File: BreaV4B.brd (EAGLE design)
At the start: 30.8 x 19 mm, 32 parts, among them J1 XF2L-0535-1, J2 XF2L-0535-1, Q3 ABM-16MHZ, SW1 ESE31L11T, SW2 EVQ11U09K, SW3 LS12T2-T, U1 TPS62200, X1 22-23-2021

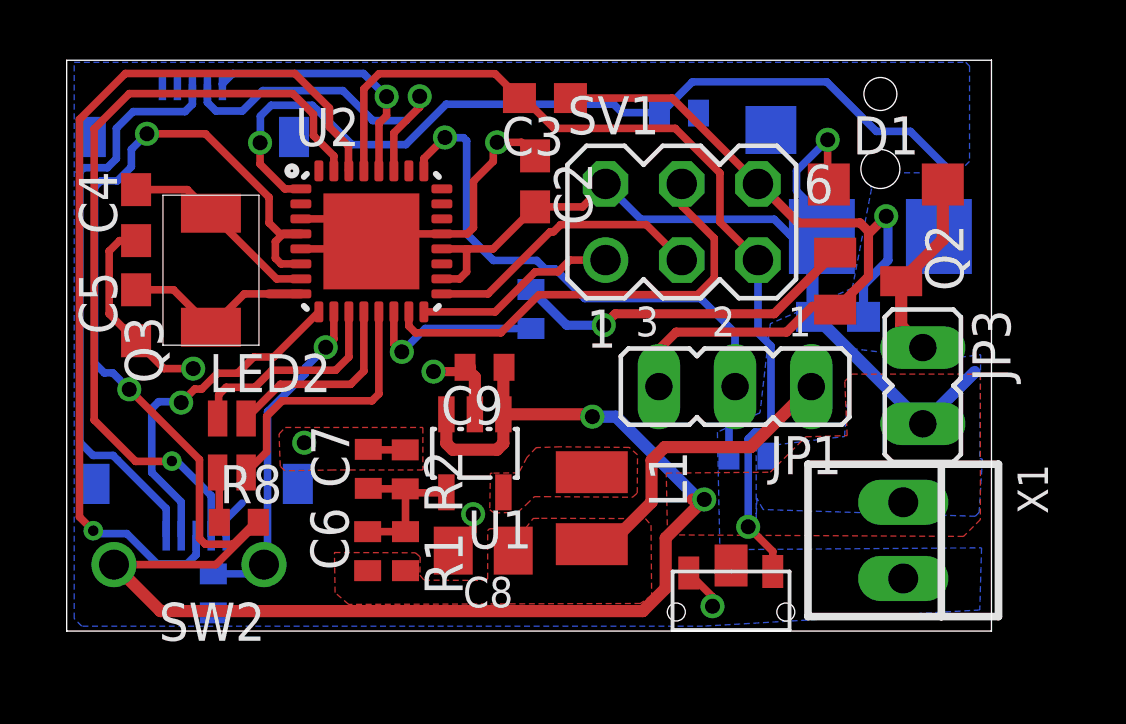
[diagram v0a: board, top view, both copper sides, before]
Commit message: Changes direction of GSM FPC. Lowered position of MQ303
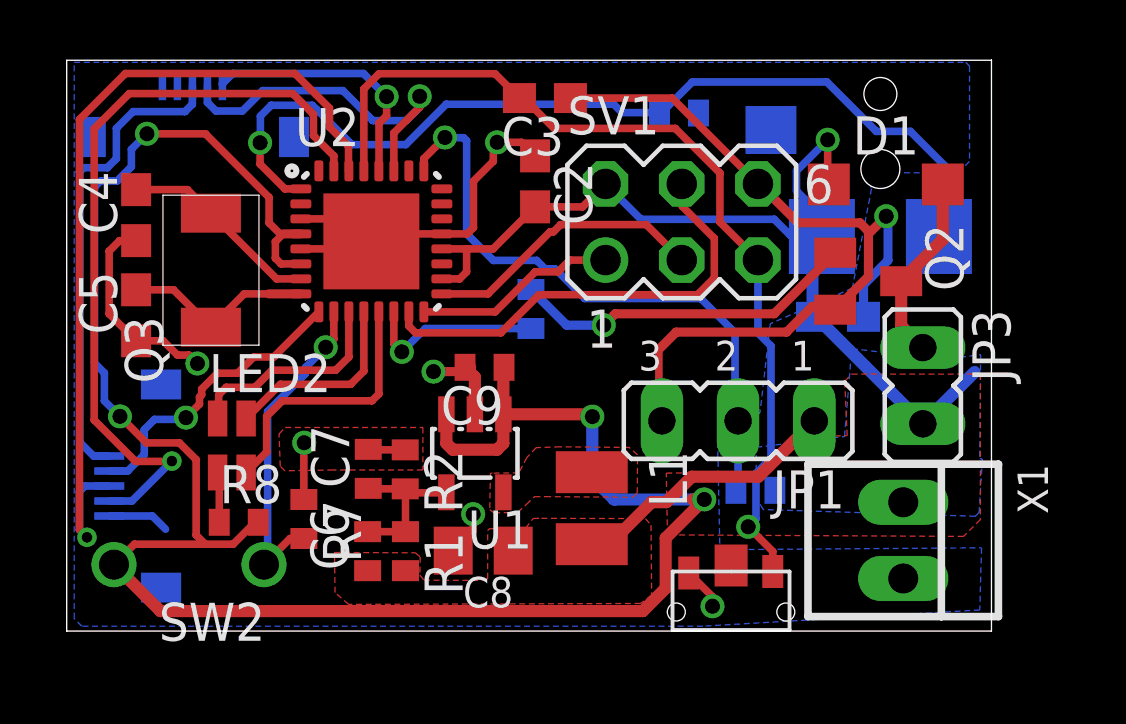
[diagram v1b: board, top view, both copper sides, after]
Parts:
- moved R7 3.91 mm to (7.91, 3.70), flipped to the top, turned to 270 degrees
- moved R3 1.16 mm to (23.0, 4.66)
- moved JP1 1.14 mm to (22.4, 6.97)
- moved J1 1.02 mm to (3.33, 4.80), turned to 0 degrees
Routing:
- net GND: track 56.5 -> 60.4 mm
- net VBATSIM: track 19.6 -> 16.1 mm
- net RX: track 30.4 -> 28.5 mm
- net REST: track 11.6 -> 9.92 mm
- net VOUT: track 10.6 -> 9.38 mm
- net N$3: track 19.8 -> 20.9 mm

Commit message: TrussKey Schematics
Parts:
- R8: value 10K -> 1K
- moved SW2 1.04 mm to (5.07, 2.50)
- moved J1 0.93 mm to (4.26, 4.87)
- moved R7 0.61 mm to (8.14, 4.26), turned to 180 degrees
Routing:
- net VCC: track 101.8 -> 100.4 mm
- net GND: track 60.4 -> 61.7 mm
- net REST: track 9.92 -> 8.90 mm
- net RX: track 28.5 -> 29.5 mm
- net VBATSIM: track 16.1 -> 17.0 mm
- net TX: track 25.9 -> 25.1 mm

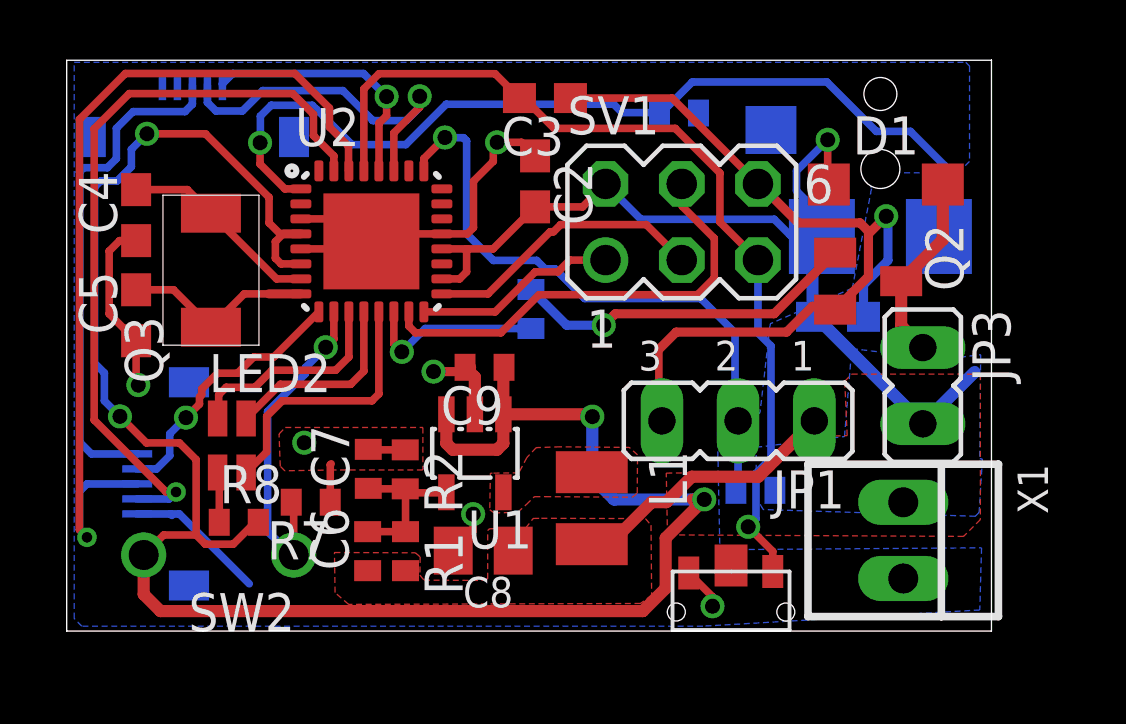
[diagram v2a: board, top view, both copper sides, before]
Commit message: Power Switch to int0
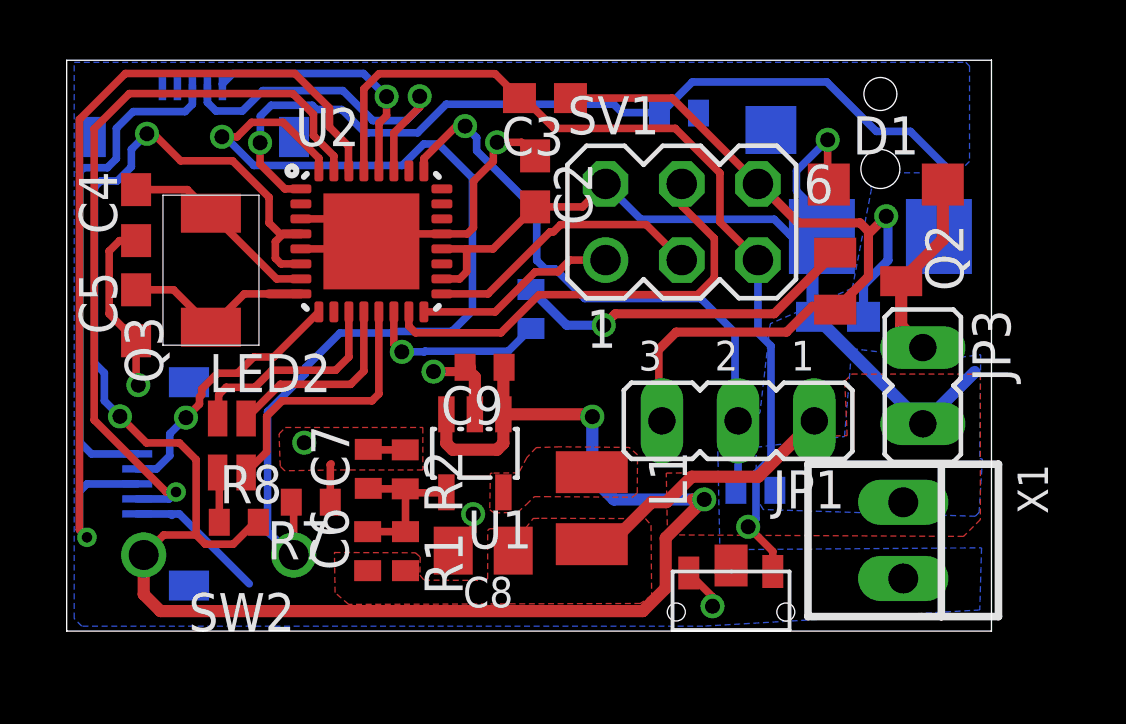
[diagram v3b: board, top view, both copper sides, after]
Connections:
- net PWRSW: now also U2.32; no longer U2.10
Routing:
- net PWRSW: track 11.2 -> 33.6 mm
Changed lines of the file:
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@@
 <wire x1="7.81" y1="13.204" x2="7.116" y2="13.204" width="0.254" layer="1"/>
 <wire x1="7.116" y1="13.204" x2="6.75" y2="13.57" width="0.254" layer="1"/>
-<wire x1="6.75" y1="13.57" x2="6.75" y2="14.42" width="0.254" layer="1"/>
-<wire x1="4.63" y1="16.54" x2="2.68" y2="16.54" width="0.254" layer="1"/>
+<wire x1="6.75" y1="14.42" x2="6.75" y2="13.57" width="0.254" layer="1"/>
 <via x="2.68" y="16.54" extent="1-16" drill="0.5"/>
 <wire x1="2.68" y1="16.54" x2="2.16" y2="16.02" width="0.254" layer="16"/>
@@
 <wire x1="0.93" y1="14.76" x2="0.93" y2="8.9" width="0.254" layer="16"/>
 <via x="1.78" y="7.12" extent="1-16" drill="0.5"/>
-<wire x1="4.63" y1="16.54" x2="6.75" y2="14.42" width="0.254" layer="1"/>
 <wire x1="21.256" y1="4.352" x2="21.0734" y2="4.352" width="0.4064" layer="16"/>
 <wire x1="20.872" y1="4.352" x2="21.256" y2="4.352" width="0.4064" layer="1"/>
@@
 <wire x1="2.57" y1="2.5" x2="3.23611875" y2="3.16611875" width="0.254" layer="1"/>
 <wire x1="3.23611875" y1="3.16611875" x2="4.31875" y2="3.16611875" width="0.254" layer="1"/>
+<wire x1="2.68" y1="16.54" x2="2.9" y2="16.54" width="0.254" layer="1"/>
+<wire x1="3.8" y1="15.64" x2="5.53" y2="15.64" width="0.254" layer="1"/>
+<wire x1="5.53" y1="15.64" x2="6.75" y2="14.42" width="0.254" layer="1"/>
+<wire x1="2.9" y1="16.54" x2="3.8" y2="15.64" width="0.254" layer="1"/>
 </signal>
 <signal name="N$1">
@@
 <contactref element="R3" pad="1"/>
 <contactref element="U2" pad="25"/>
-<via x="12.613" y="16.417" extent="1-16" drill="0.5"/>
+<via x="13.283" y="16.797" extent="1-16" drill="0.5"/>
 <wire x1="17.272" y1="11.049" x2="21.141" y2="11.049" width="0.254" layer="16"/>
-<wire x1="14.224" y1="12.319" x2="13.335" y2="13.208" width="0.254" layer="16"/>
-<wire x1="14.224" y1="12.319" x2="15.6718" y2="12.319" width="0.254" layer="16"/>
 <wire x1="15.6718" y1="12.319" x2="15.9512" y2="12.0396" width="0.254" layer="16"/>
 <wire x1="15.9512" y1="12.0396" x2="16.2814" y2="12.0396" width="0.254" layer="16"/>
@@
 <wire x1="21.141" y1="11.049" x2="22.284" y2="9.906" width="0.254" layer="16"/>
 <wire x1="11.91" y1="15.304" x2="11.91" y2="15.714" width="0.254" layer="1"/>
-<wire x1="11.91" y1="15.714" x2="12.613" y2="16.417" width="0.254" layer="1"/>
-<wire x1="13.335" y1="13.208" x2="13.335" y2="16.305" width="0.254" layer="16"/>
-<wire x1="13.335" y1="16.305" x2="13.23" y2="16.41" width="0.254" layer="16"/>
-<wire x1="13.23" y1="16.41" x2="12.62" y2="16.41" width="0.254" layer="16"/>
-<wire x1="12.62" y1="16.41" x2="12.613" y2="16.417" width="0.254" layer="16"/>
 <wire x1="22.284" y1="9.906" x2="22.284" y2="7.072" width="0.254" layer="16"/>
 <wire x1="22.284" y1="7.072" x2="22.384" y2="6.972" width="0.254" layer="16"/>
 <wire x1="22.384" y1="6.972" x2="22.384" y2="4.73" width="0.254" layer="16"/>
 <wire x1="22.384" y1="4.73" x2="22.309" y2="4.655" width="0.254" layer="16"/>
+<wire x1="11.91" y1="15.714" x2="12.993" y2="16.797" width="0.254" layer="1"/>
+<wire x1="12.993" y1="16.797" x2="13.283" y2="16.797" width="0.254" layer="1"/>
+<wire x1="13.283" y1="16.797" x2="13.6692" y2="16.4108" width="0.254" layer="16"/>
+<wire x1="13.6692" y1="16.4108" x2="13.6692" y2="15.9735875" width="0.254" layer="16"/>
+<wire x1="15.6718" y1="13.9709875" x2="15.6718" y2="12.319" width="0.254" layer="16"/>
+<wire x1="13.6692" y1="15.9735875" x2="15.6718" y2="13.9709875" width="0.254" layer="16"/>
 </signal>
 <signal name="SW">
@@
 <signal name="SOL">
 <contactref element="R5" pad="2"/>
-<wire x1="15.479" y1="10.05" x2="11.955" y2="10.05" width="0.254" layer="16"/>
-<wire x1="11.955" y1="10.05" x2="11.176" y2="9.271" width="0.254" layer="16"/>
 <via x="11.176" y="9.271" extent="1-16" drill="0.5"/>
 <contactref element="U2" pad="14"/>
 <wire x1="10.91" y1="10.604" x2="10.91" y2="9.537" width="0.254" layer="1"/>
 <wire x1="10.91" y1="9.537" x2="11.176" y2="9.271" width="0.254" layer="1"/>
+<wire x1="11.176" y1="9.271" x2="11.9247875" y2="9.271" width="0.254" layer="16"/>
+<wire x1="11.9247875" y1="9.271" x2="11.9485875" y2="9.2948" width="0.254" layer="16"/>
+<wire x1="14.7238" y1="9.2948" x2="15.479" y2="10.05" width="0.254" layer="16"/>
+<wire x1="11.9485875" y1="9.2948" x2="14.7238" y2="9.2948" width="0.254" layer="16"/>
 </signal>
 <signal name="N$9">
@@
 <wire x1="28.13" y1="16.62" x2="29.28" y2="15.47" width="0.254" layer="16"/>
 <contactref element="U2" pad="1"/>
-<wire x1="18.2372" y1="17.526" x2="12.656" y2="17.526" width="0.254" layer="16"/>
-<wire x1="12.656" y1="17.526" x2="11.31" y2="16.18" width="0.254" layer="16"/>
-<wire x1="11.31" y1="16.18" x2="9.51" y2="16.18" width="0.254" layer="16"/>
-<wire x1="9.51" y1="16.18" x2="8.34" y2="17.35" width="0.254" layer="16"/>
-<wire x1="8.34" y1="17.35" x2="8.33" y2="17.35" width="0.254" layer="16"/>
-<wire x1="8.33" y1="17.35" x2="8.19" y2="17.49" width="0.254" layer="16"/>
+<wire x1="12.656" y1="17.526" x2="18.2372" y2="17.526" width="0.254" layer="16"/>
+<wire x1="8.19" y1="17.49" x2="8.33" y2="17.35" width="0.254" layer="16"/>
 <wire x1="8.19" y1="17.49" x2="6.82" y2="17.49" width="0.254" layer="16"/>
 <wire x1="7.81" y1="14.704" x2="7.276" y2="14.704" width="0.254" layer="1"/>
@@
 <wire x1="6.45" y1="16.24" x2="6.45" y2="15.53" width="0.254" layer="1"/>
 <wire x1="6.45" y1="15.53" x2="7.276" y2="14.704" width="0.254" layer="1"/>
+<wire x1="9.17" y1="17.35" x2="9.94" y2="16.58" width="0.254" layer="16"/>
+<wire x1="9.94" y1="16.58" x2="10.0352625" y2="16.58" width="0.254" layer="16"/>
+<wire x1="10.0352625" y1="16.58" x2="10.0416625" y2="16.5736" width="0.254" layer="16"/>
+<wire x1="10.0416625" y1="16.5736" x2="11.7036" y2="16.5736" width="0.254" layer="16"/>
+<wire x1="11.7036" y1="16.5736" x2="12.656" y2="17.526" width="0.254" layer="16"/>
+<wire x1="8.33" y1="17.35" x2="9.17" y2="17.35" width="0.254" layer="16"/>
 </signal>
 <signal name="SDA">
@@
 <contactref element="R7" pad="2"/>
 <contactref element="SW2" pad="P$1"/>
-<contactref element="U2" pad="10"/>
-<via x="8.638" y="9.425" extent="1-16" drill="0.5"/>
-<wire x1="8.91" y1="10.604" x2="8.91" y2="9.697" width="0.254" layer="1"/>
-<wire x1="8.91" y1="9.697" x2="8.638" y2="9.425" width="0.254" layer="1"/>
 <wire x1="7.96" y1="8.54" x2="6.7" y2="7.28" width="0.254" layer="16"/>
 <wire x1="7.96" y1="8.54" x2="7.96" y2="8.747" width="0.254" layer="16"/>
-<wire x1="7.96" y1="8.747" x2="8.638" y2="9.425" width="0.254" layer="16"/>
 <wire x1="6.7" y1="7.28" x2="6.7" y2="3.27" width="0.254" layer="16"/>
 <wire x1="6.7" y1="3.27" x2="7.57" y2="2.5" width="0.254" layer="16"/>
 <wire x1="7.49" y1="4.26" x2="7.57" y2="4.18" width="0.254" layer="1"/>
 <wire x1="7.57" y1="4.18" x2="7.57" y2="2.5" width="0.254" layer="1"/>
+<contactref element="U2" pad="32"/>
+<wire x1="7.96" y1="8.747" x2="9.113" y2="9.9" width="0.254" layer="16"/>
+<wire x1="13.53" y1="10.64" x2="13.53" y2="15.07" width="0.254" layer="16"/>
+<wire x1="13.53" y1="15.07" x2="12.4" y2="16.2" width="0.254" layer="16"/>
+<wire x1="12.4" y1="16.2" x2="11.9047375" y2="16.2" width="0.254" layer="16"/>
+<wire x1="11.9047375" y1="16.2" x2="11.1893375" y2="15.4846" width="0.254" layer="16"/>
+<wire x1="11.1893375" y1="15.4846" x2="6.2411875" y2="15.4846" width="0.254" layer="16"/>
+<via x="5.18" y="16.44" extent="1-16" drill="0.5"/>
+<wire x1="9.113" y1="9.9" x2="10.8407875" y2="9.9" width="0.254" layer="16"/>
+<wire x1="8.41" y1="15.7252625" x2="8.41" y2="15.304" width="0.254" layer="1"/>
+<wire x1="10.8407875" y1="9.9" x2="10.8935875" y2="9.9528" width="0.254" layer="16"/>
+<wire x1="12.8428" y1="9.9528" x2="13.53" y2="10.64" width="0.254" layer="16"/>
+<wire x1="10.8935875" y1="9.9528" x2="12.8428" y2="9.9528" width="0.254" layer="16"/>
+<wire x1="5.18" y1="16.44" x2="5.6857875" y2="16.44" width="0.254" layer="1"/>
+<wire x1="5.6857875" y1="16.44" x2="6.1675875" y2="16.9218" width="0.254" layer="1"/>
+<wire x1="6.1675875" y1="16.9218" x2="7.2134625" y2="16.9218" width="0.254" layer="1"/>
+<wire x1="7.2134625" y1="16.9218" x2="8.41" y2="15.7252625" width="0.254" layer="1"/>
+<wire x1="5.2857875" y1="16.44" x2="5.18" y2="16.44" width="0.254" layer="16"/>
+<wire x1="6.2411875" y1="15.4846" x2="5.2857875" y2="16.44" width="0.254" layer="16"/>
 </signal>
 <signal name="VBATSIM">

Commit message: Rx Tx
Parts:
- moved J2 0.23 mm to (4.16, 16.0)
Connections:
- net RX: now also J1.4; no longer J1.3
- net TX: now also J1.3; no longer J1.4
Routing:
- net RX: track 29.5 -> 26.1 mm
- net PWRSW: track 33.6 -> 31.1 mm
- net TX: track 25.1 -> 23.1 mm
- net DETSW: track 31.2 -> 33.1 mm
- net VCC: track 100.4 -> 99.8 mm
- net SDA: track 11.9 -> 12.4 mm
